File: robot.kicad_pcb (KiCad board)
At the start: 2 copper layers, 84 x 70 mm, 23 parts, among them P1 CONN_01X03, P2 CONN_01X03, P3 CONN_01X08, P4 CONN_01X08, P5 CONN_01X03, P7 CONN_01X08, Q1 BC548, U1 AMS1117-3V3, U2 ESP32-WROOM

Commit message: Ajuste na face do esp
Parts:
- U1, U2: moved to B.Cu
- moved U1 15.1 mm to (148.7, 98.9)
- moved Output+1 9.31 mm to (192.3, 148.4)
- moved Output-1 8.79 mm to (192.3, 139.0)
- moved Motor1 5.85 mm to (178.0, 105.1), turned to 270 degrees
- moved Motor2 2.35 mm to (186.2, 105.0)
- moved U2 0.77 mm to (152.2, 119.0), turned to 0 degrees
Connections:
- Input+1 pad 1: Vin -> Net-(Input+1-Pad1)
- Input-1 pad 1: GND -> Vin
- Input-1 pad 2: Net-(Input-1-Pad2) -> GND
- Output+1 pad 2: VM -> Net-(Output+1-Pad2)
- Output-1 pad 1: Net-(Output-1-Pad1) -> VM
- U1 pad 3: Vin -> VM
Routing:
- net Vin: track 207.7 -> 70.8 mm
- net VM: track 11.1 -> 106.2 mm
- net Net-(U1-Pad2): track 0.00 -> 42.1 mm
- net SCL: track 23.7 -> 4.08 mm
- net AIN1: track 0.00 -> 19.6 mm
- net PWMB: track 11.7 -> 0.00 mm
- net PWMA: track 11.6 -> 2.09 mm
- net INT: track 19.3 -> 28.8 mm
- net SDA: track 22.9 -> 13.9 mm
- net Net-(U2-Pad28): track 0.00 -> 9.00 mm
- net BUZZER: track 82.0 -> 90.5 mm
- net BI1: track 12.9 -> 4.44 mm
- net Net-(Motor1-Pad1): track 29.1 -> 22.3 mm
- net Net-(Motor2-Pad2): track 19.4 -> 17.0 mm
- net Net-(Motor2-Pad1): track 14.7 -> 12.3 mm
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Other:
- outline, holes or cut-outs redrawn

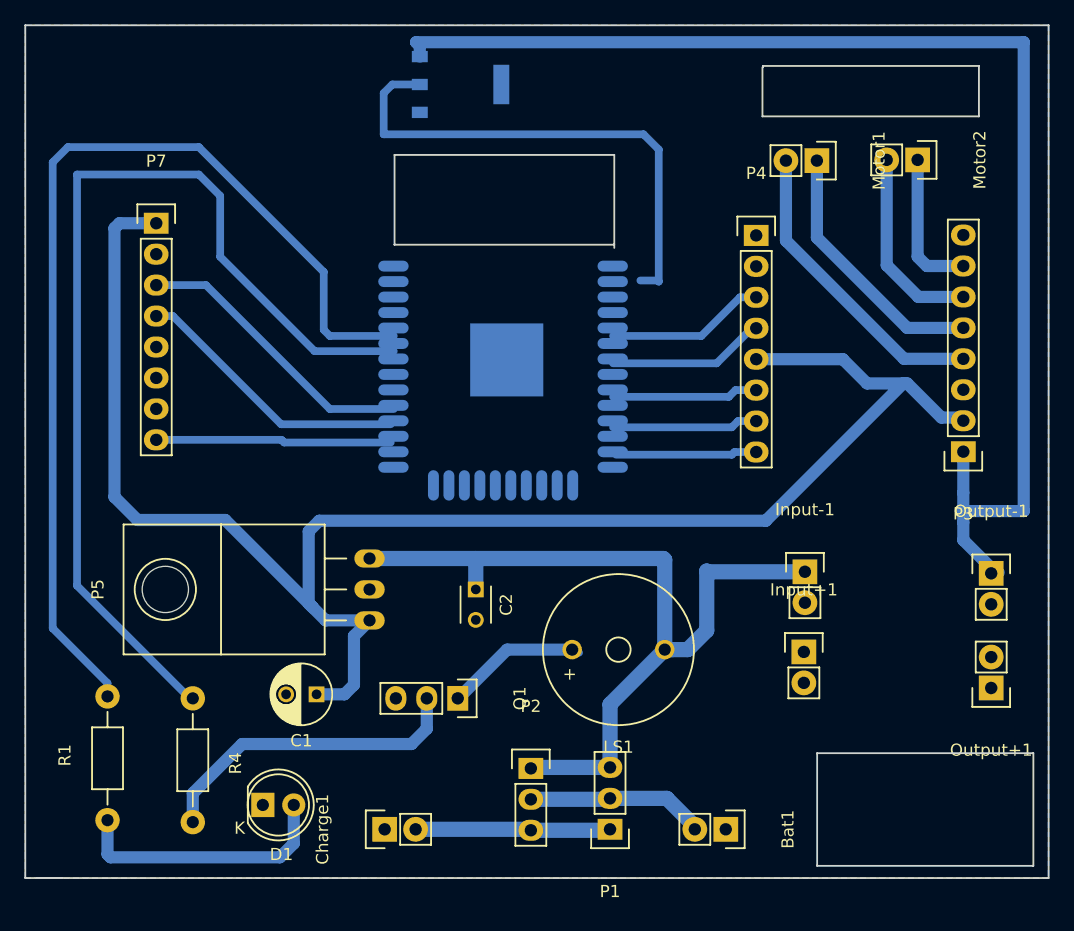
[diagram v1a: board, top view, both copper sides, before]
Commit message: mudanças na dimensão da placa.
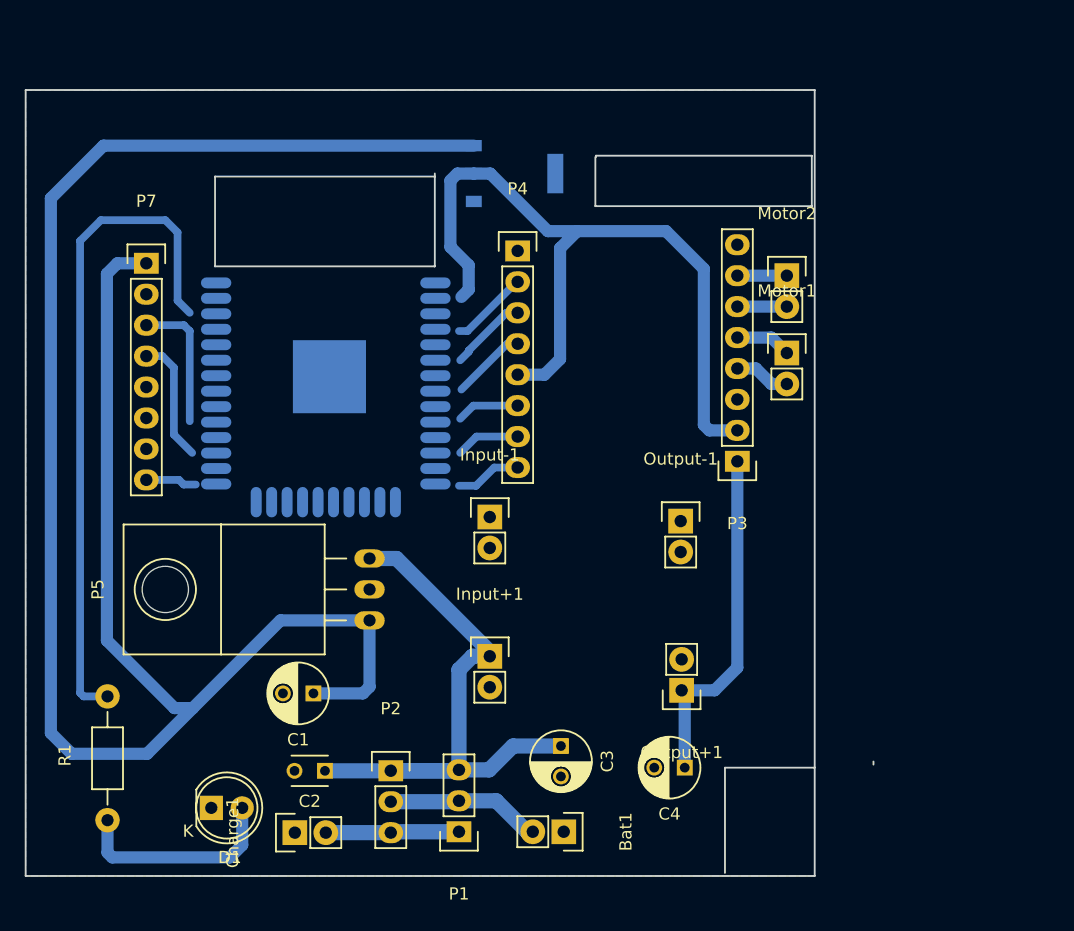
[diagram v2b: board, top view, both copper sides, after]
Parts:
- removed LS1: MCKPM-G1201A-K4037, Buzzers_Beepers:MagneticBuzzer_ProSignal_ABI-009-RC
- removed Q1: BC548, Pin_Headers:Pin_Header_Straight_1x03
- removed R4: 2K2, Resistors_ThroughHole:Resistor_Horizontal_RM10mm
- added C3: 100uF, Capacitors_ThroughHole:C_Radial_D5_L11_P2.5, F.Cu at (157.0, 153.2)
- added C4: 10uF, Capacitors_ThroughHole:C_Radial_D5_L11_P2.5, F.Cu at (167.1, 154.9)
- moved Input-1 26.3 mm to (151.1, 134.4)
- moved Output-1 25.8 mm to (166.8, 134.7)
- moved Input+1 25.8 mm to (151.1, 145.8)
- moved Output+1 25.4 mm to (166.9, 148.6)
- moved P4 19.6 mm to (153.4, 112.5)
- moved C2 19.4 mm to (137.6, 155.2), turned to 180 degrees
- moved P3 18.6 mm to (171.4, 129.8)
- moved Motor1 16.0 mm to (175.5, 120.9), turned to 0 degrees
- moved U2 14.6 mm to (137.7, 120.4)
- moved Motor2 14.3 mm to (175.5, 114.6), turned to 0 degrees
- moved Bat1 13.3 mm to (157.2, 160.2)
- moved P1 12.4 mm to (148.6, 160.2)
- moved P2 11.5 mm to (143.0, 155.2)
- moved U1 8.55 mm to (153.2, 106.2)
- moved Charge1 7.38 mm to (135.1, 160.3)
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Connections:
- C1 pad 1: Vcc -> Net-(C1-Pad1)
- Input+1 pad 1: Net-(Input+1-Pad1) -> Vin
- Input-1 pad 1: Vin -> GND
- Input-1 pad 2: GND -> Net-(Input-1-Pad2)
- Output+1 pad 1: Net-(Output+1-Pad1) -> VM
- Output-1 pad 1: VM -> GND
- Output-1 pad 2: GND -> Net-(Output-1-Pad2)
- P5 pad 1: Vcc -> Net-(C1-Pad1)
- P7 pad 1: Vcc -> Net-(C1-Pad1)
- U1 pad 2: Net-(U1-Pad2) -> Vcc
- U1 pad 3: VM -> Net-(C1-Pad1)
- U2 pad 10: Net-(U2-Pad10) -> AIN1
- U2 pad 11: SCL -> Net-(U2-Pad11)
- U2 pad 12: SDA -> AIN2
- U2 pad 13: INT -> Net-(U2-Pad13)
- U2 pad 14: Net-(U2-Pad14) -> PWMA
- U2 pad 2: Net-(U1-Pad2) -> Vcc
- U2 pad 25: PWMA -> INT
- U2 pad 27: AIN2 -> SDA
- U2 pad 29: AIN1 -> SCL
- U2 pad 31: BIN1 -> BUZZER
- U2 pad 33: BIN2 -> Net-(U2-Pad33)
- U2 pad 36: Net-(U2-Pad36) -> LED
- U2 pad 37: PWMB -> Net-(U2-Pad37)
- U2 pad 4: Net-(U2-Pad4) -> PWMB
- U2 pad 6: LED -> BIN2
- U2 pad 7: BUZZER -> Net-(U2-Pad7)
- U2 pad 8: Net-(U2-Pad8) -> BIN1
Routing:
- net Net-(C1-Pad1): track 0.00 -> 165.1 mm
- net BUZZER: track 90.5 -> 0.00 mm
- net VM: track 106.2 -> 28.7 mm
- net Vcc: track 140.5 -> 65.5 mm
- net Net-(U1-Pad2): track 42.1 -> 0.00 mm
- net LED: track 83.4 -> 55.6 mm
- net Net-(Q1-Pad2): track 26.3 -> 0.00 mm
- net INT: track 28.8 -> 4.22 mm
- net Net-(Motor1-Pad2): track 25.1 -> 4.59 mm
- net Vin: track 70.8 -> 50.5 mm
- net AIN1: track 19.6 -> 0.00 mm
- net Net-(Motor1-Pad1): track 22.3 -> 4.59 mm
- net Net-(Motor2-Pad2): track 17.0 -> 4.06 mm
- net Net-(LS1-Pad2): track 11.8 -> 0.00 mm
- net Net-(U2-Pad28): track 9.00 -> 0.00 mm
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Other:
- board size 84 x 70 mm -> 69.6 x 64.5 mm

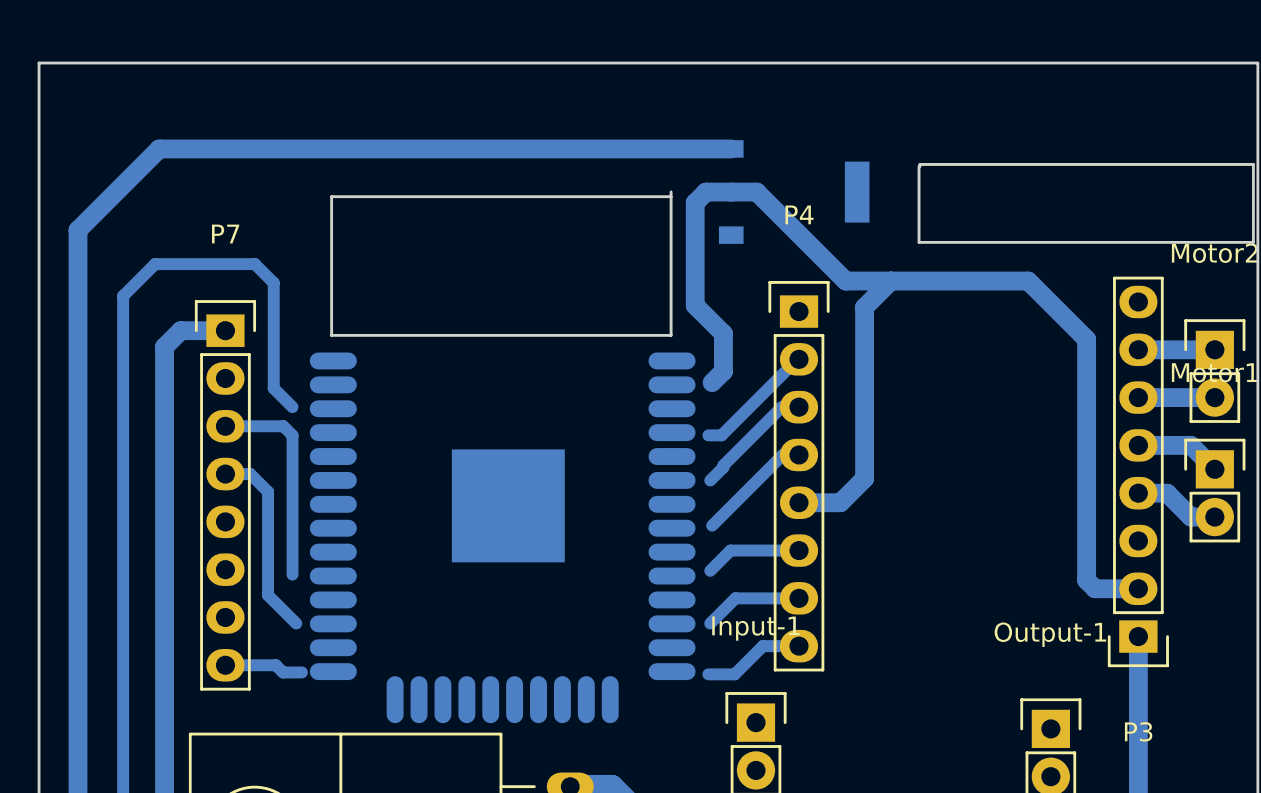
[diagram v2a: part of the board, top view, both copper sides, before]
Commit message: corrigir gnd da ponte H
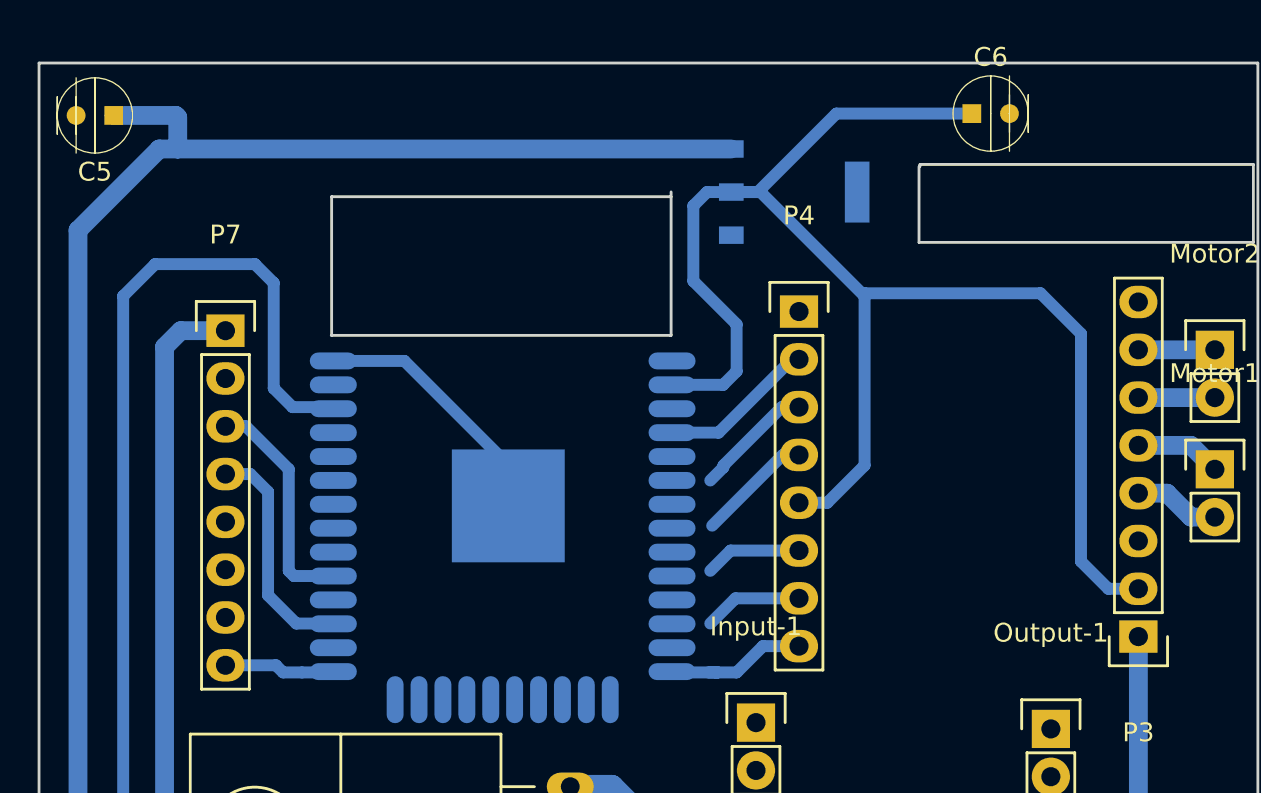
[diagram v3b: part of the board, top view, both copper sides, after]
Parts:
- added C5: 100uF, Capacitors_ThroughHole:C_Radial_D5_L11_P2.5, F.Cu at (117.0, 102.1)
- added C6: 10uF, Capacitors_ThroughHole:C_Radial_D5_L11_P2.5, F.Cu at (162.6, 102.0)
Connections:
- U2 pad 38: Net-(U2-Pad38) -> GND
- U2 pad 39: Net-(U2-Pad39) -> GND
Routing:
- net Vcc: track 65.5 -> 81.4 mm
- net GND: track 0.00 -> 15.5 mm
- net Net-(C1-Pad1): track 165.1 -> 170.3 mm
- net PWMA: track 5.44 -> 7.85 mm
- net LED: track 55.6 -> 57.8 mm
- net SDA: track 10.3 -> 12.3 mm
- net PWMB: track 6.87 -> 8.82 mm
- net INT: track 4.22 -> 5.91 mm
- net SCL: track 11.2 -> 12.2 mm
